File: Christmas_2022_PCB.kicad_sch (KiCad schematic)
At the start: 19 parts, among them J1 USB_A, SW1 SW_Push, SW2 SW_Push, U1 STM32F030K6Tx, U2 AMS1117-3.3

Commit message: initialised PCB
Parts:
- BT1: renamed from BT?; value Battery_Cell -> (none)
- D1, D2, D3, D4, D5: value LED -> (none)
- J1: value USB_A -> (none)
- R1, R10, R4, R5, R6, R7, R8, R9: value R -> (none)
- SW1, SW2: value SW_Push -> (none)
- U1: value STM32F030K6Tx -> (none); footprint Package_QFP:LQFP-32_7x7mm_P0.8mm -> (none)
- U2: value AMS1117-3.3 -> (none); footprint Package_TO_SOT_SMD:SOT-223-3_TabPin2 -> (none)

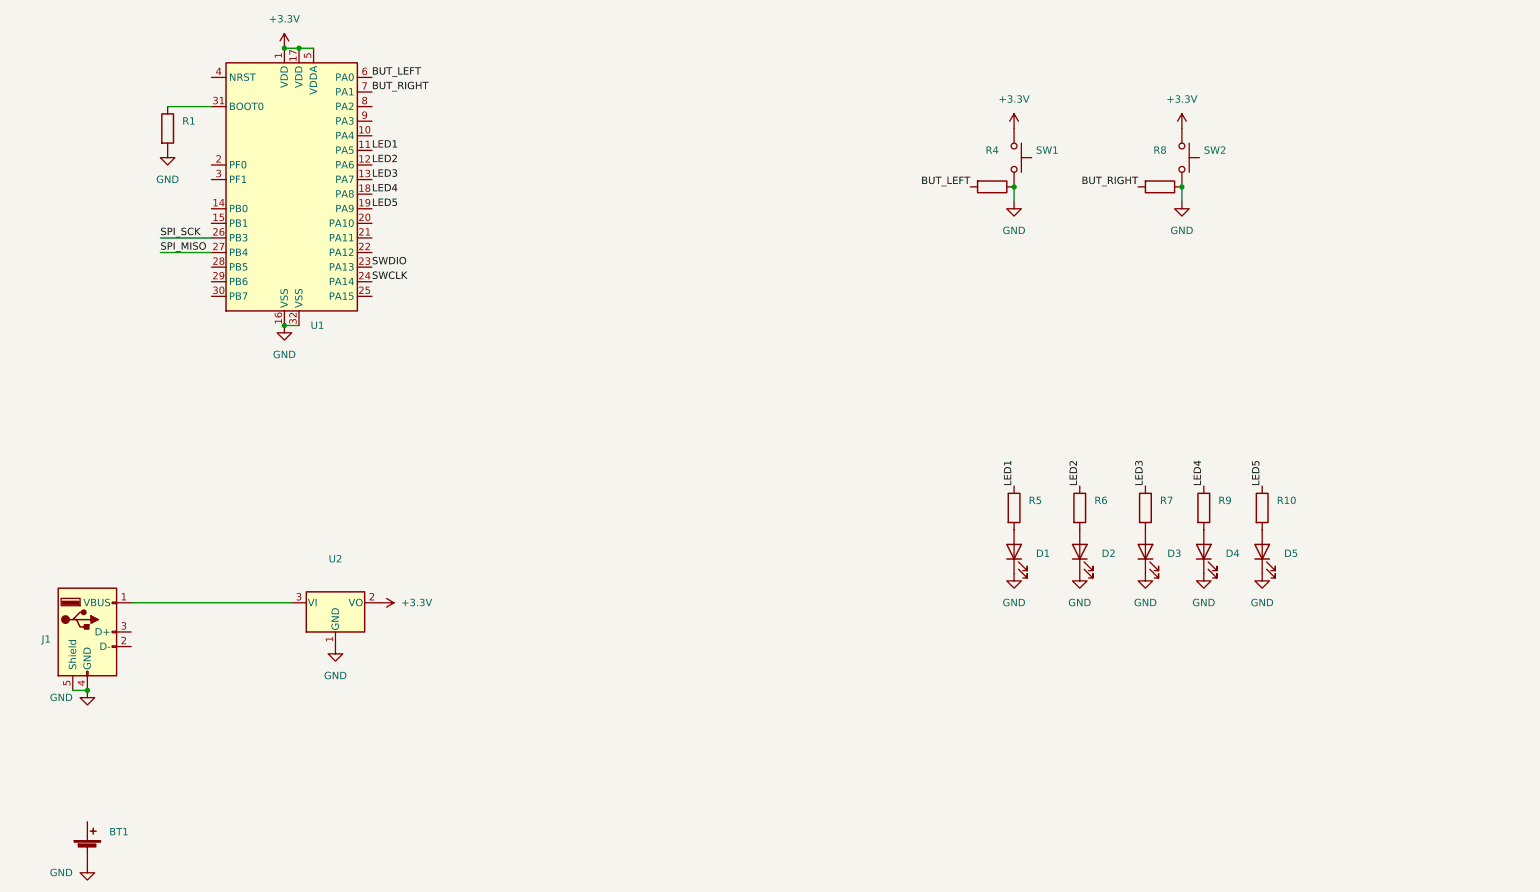
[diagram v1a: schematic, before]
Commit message: Added 3.3V slide switch
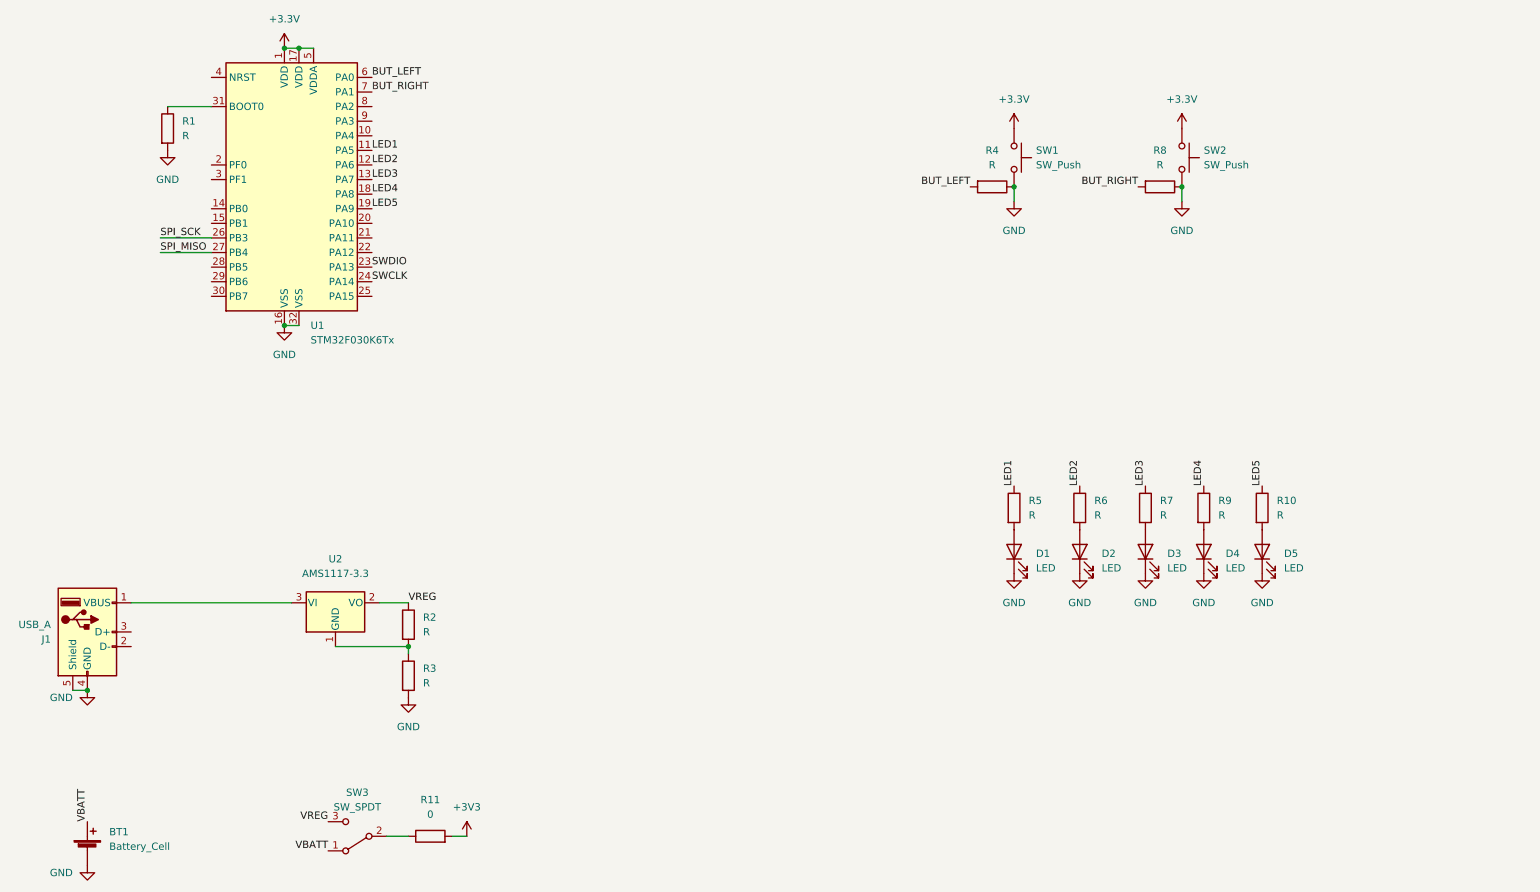
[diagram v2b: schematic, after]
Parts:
- added R11: 0, Resistor_SMD:R_0805_2012Metric_Pad1.20x1.40mm_HandSolder, symbol Device:R
- added R2, R3: R, Resistor_SMD:R_0805_2012Metric_Pad1.20x1.40mm_HandSolder, symbol Device:R
- added SW3: SW_SPDT, Button_Switch_SMD:SW_SPDT_PCM12, symbol Switch:SW_SPDT
- BT1: value (none) -> Battery_Cell; footprint (none) -> Battery:BatteryHolder_Keystone_3034_1x20mm
- D1, D2, D3, D4, D5: value (none) -> LED; footprint (none) -> LED_SMD:LED_0805_2012Metric_Pad1.15x1.40mm_HandSolder
- J1: value (none) -> USB_A; footprint (none) -> Connector_USB:USB_A_CNCTech_1001-011-01101_Horizontal
- R1, R10, R4, R5, R6, R7, R8, R9: value (none) -> R; footprint (none) -> Resistor_SMD:R_0805_2012Metric_Pad1.20x1.40mm_HandSolder
- SW1, SW2: value (none) -> SW_Push; footprint (none) -> Library:3_6_2_5mm_push_button_G_lead
- U1: value (none) -> STM32F030K6Tx; footprint (none) -> Package_QFP:LQFP-32_7x7mm_P0.8mm
- U2: value (none) -> AMS1117-3.3; footprint (none) -> Package_TO_SOT_SMD:SOT-223-3_TabPin2
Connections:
- net +3V3: now also R11.2; no longer U2.2 (VO)
- net GND: now also R3.2; no longer U2.1 (GND)
- net VBATT: now reaches BT1.1 (+)
- net VBATT: now also SW3.1 (A)
- new net: R2.2, R3.1, U2.1 (GND)
- new net: R11.1, SW3.2 (B)
- new net VREG: R2.1, SW3.3 (C), U2.2 (VO)

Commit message: completed initial layout
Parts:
- added C1, C2, C3: (no value), symbol Device:C
- added D6, D7: (no value), symbol Device:LED
- added R12, R13: (no value), symbol Device:R
- BT1: value Battery_Cell -> (none); footprint Battery:BatteryHolder_Keystone_3034_1x20mm -> (none)
- D1, D2, D3, D4, D5: value LED -> (none); footprint LED_SMD:LED_0805_2012Metric_Pad1.15x1.40mm_HandSolder -> (none)
- J1: value USB_A -> (none); footprint Connector_USB:USB_A_CNCTech_1001-011-01101_Horizontal -> (none)
- R1, R10, R2, R3, R4, R5, R6, R7, R9: value R -> (none); footprint Resistor_SMD:R_0805_2012Metric_Pad1.20x1.40mm_HandSolder -> (none)
- R11: value 0 -> (none); footprint Resistor_SMD:R_0805_2012Metric_Pad1.20x1.40mm_HandSolder -> (none)
- SW1: value SW_Push -> (none); footprint Library:3_6_2_5mm_push_button_G_lead -> (none)
- SW3: value SW_SPDT -> (none); footprint Button_Switch_SMD:SW_SPDT_PCM12 -> (none)
- U1: value STM32F030K6Tx -> (none); footprint Package_QFP:LQFP-32_7x7mm_P0.8mm -> (none)
- U2: value AMS1117-3.3 -> (none); footprint Package_TO_SOT_SMD:SOT-223-3_TabPin2 -> (none)
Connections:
- net +3V3: now also C1.1, C2.1, C3.1
- net BUT_LEFT: now also SW1.2
- net BUT_RIGHT: now also SW2.2
- net GND: now also C1.2, C2.2, C3.2, D6.1 (K), D7.1 (K); no longer SW1.2, SW2.2
- net LED6: now reaches U1.20 (PA10)
- net LED6: now also R12.1
- net LED7: now reaches U1.21 (PA11)
- net LED7: now also R13.1
- new net: D6.2 (A), R12.2
- new net: D7.2 (A), R13.2
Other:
- moved on the sheet: R4

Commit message: began routing
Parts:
- added J2, J3: SOP8_test_point, Library:sop_8_test_pad, symbol New_Library:SOP8_test_point
- R8: value R -> (none); footprint Resistor_SMD:R_0805_2012Metric_Pad1.20x1.40mm_HandSolder -> (none)
- SW2: value SW_Push -> (none); footprint Library:3_6_2_5mm_push_button_G_lead -> (none)
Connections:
- net +3V3: now also J2.1
- net GND: now also J2.2
- net SWCLK: now also J2.3
- net SWDIO: now also J2.4
- net NRST: now reaches U1.4 (NRST)
- net NRST: now also J3.2
- no-connect marks 0 -> 15
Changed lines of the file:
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@@
   (junction (at 66.04 35.56) (diameter 0) (color 0 0 0 0)
   )
+  (no_connect (at 78.74 45.72))
+  (no_connect (at 78.74 48.26))
+  (no_connect (at 78.74 50.8))
+  (no_connect (at 50.8 55.88))
+  (no_connect (at 50.8 58.42))
+  (no_connect (at 111.76 110.49))
+  (no_connect (at 111.76 115.57))
+  (no_connect (at 111.76 118.11))
+  (no_connect (at 50.8 73.66))
+  (no_connect (at 50.8 63.5))
+  (no_connect (at 50.8 66.04))
+  (no_connect (at 78.74 71.12))
+  (no_connect (at 78.74 78.74))
+  (no_connect (at 50.8 76.2))
+  (no_connect (at 50.8 78.74))
   (wire (pts (xy 29.21 147.32) (xy 26.67 147.32))
     (stroke (width 0) (type default) (color 0 0 0 0))
@@
     (stroke (width 0) (type default) (color 0 0 0 0))
   )
+  (wire (pts (xy 107.95 95.25) (xy 111.76 95.25))
+    (stroke (width 0) (type default) (color 0 0 0 0))
+  )
   (wire (pts (xy 80.01 132.08) (xy 85.09 132.08))
     (stroke (width 0) (type default) (color 0 0 0 0))
@@
     (stroke (width 0) (type default) (color 0 0 0 0))
   )
+  (wire (pts (xy 100.33 97.79) (xy 111.76 97.79))
+    (stroke (width 0) (type default) (color 0 0 0 0))
+  )
   (wire (pts (xy 92.71 172.72) (xy 95.25 172.72))
     (stroke (width 0) (type default) (color 0 0 0 0))
@@
     (stroke (width 0) (type default) (color 0 0 0 0))
   )
+  (wire (pts (xy 107.95 93.98) (xy 107.95 95.25))
+    (stroke (width 0) (type default) (color 0 0 0 0))
+  )
   (label "SPI_MISO" (at 41.91 71.12 0)
     (effects (font (size 1.27 1.27)) (justify left bottom))
@@
     (effects (font (size 1.27 1.27)) (justify left bottom))
   )
+  (label "SWCLK" (at 111.76 100.33 180)
+    (effects (font (size 1.27 1.27)) (justify right bottom))
+  )
+  (label "NRST" (at 111.76 113.03 180)
+    (effects (font (size 1.27 1.27)) (justify right bottom))
+  )
   (label "LED4" (at 223.52 111.76 90)
     (effects (font (size 1.27 1.27)) (justify left bottom))
@@
   (label "VBATT" (at 29.21 170.18 90)
     (effects (font (size 1.27 1.27)) (justify left bottom))
+  )
+  (label "NRST" (at 50.8 40.64 180)
+    (effects (font (size 1.27 1.27)) (justify right bottom))
   )
   (label "BUT_RIGHT" (at 212.09 59.69 180)
@@
     (effects (font (size 1.27 1.27)) (justify left bottom))
   )
+  (label "SWDIO" (at 111.76 102.87 180)
+    (effects (font (size 1.27 1.27)) (justify right bottom))
+  )
   (label "LED2" (at 201.93 111.76 90)
     (effects (font (size 1.27 1.27)) (justify left bottom))
@@
       (effects (font (size 1.27 1.27)) (justify right))
     )
-    (property "Value" "R" (id 1) (at 222.25 64.7699 0)
-      (effects (font (size 1.27 1.27)) (justify right))
-    )
-    (property "Footprint" "Resistor_SMD:R_0805_2012Metric_Pad1.20x1.40mm_HandSolder" (id 2) (at 221.488 63.5 90)
+    (property "Value" "" (id 1) (at 222.25 64.7699 0)
+      (effects (font (size 1.27 1.27)) (justify right))
+    )
+    (property "Footprint" "" (id 2) (at 221.488 63.5 90)
       (effects (font (size 1.27 1.27)) hide)
     )
@@
     (pin "1")
   )
+  (symbol (lib_id "New_Library:SOP8_test_point") (at 116.84 100.33 0) (unit 1)
+    (in_bom yes) (on_board yes) (fields_autoplaced)
+    (property "Reference" "J2" (id 0) (at 123.19 99.0599 0)
+      (effects (font (size 1.27 1.27)) (justify left))
+    )
+    (property "Value" "SOP8_test_point" (id 1) (at 123.19 101.5999 0)
+      (effects (font (size 1.27 1.27)) (justify left))
+    )
+    (property "Footprint" "Library:sop_8_test_pad" (id 2) (at 127 91.44 0)
+      (effects (font (size 1.27 1.27)) hide)
+    )
+    (property "Datasheet" "" (id 3) (at 116.84 100.33 0)
+      (effects (font (size 1.27 1.27)) hide)
+    )
+    (pin "2")
+    (pin "3")
+    (pin "4")
+    (pin "1")
+  )
   (symbol (lib_id "power:GND") (at 29.21 177.8 0) (unit 1)
     (in_bom yes) (on_board yes) (fields_autoplaced)
@@
     (pin "1")
   )
+  (symbol (lib_id "power:+3.3V") (at 107.95 93.98 0) (unit 1)
+    (in_bom yes) (on_board yes) (fields_autoplaced)
+    (property "Reference" "#PWR023" (id 0) (at 107.95 97.79 0)
+      (effects (font (size 1.27 1.27)) hide)
+    )
+    (property "Value" "+3.3V" (id 1) (at 107.95 88.9 0))
+    (property "Footprint" "" (id 2) (at 107.95 93.98 0)
+      (effects (font (size 1.27 1.27)) hide)
+    )
+    (property "Datasheet" "" (id 3) (at 107.95 93.98 0)
+      (effects (font (size 1.27 1.27)) hide)
+    )
+    (pin "1")
+  )
   (symbol (lib_id "Device:C") (at 115.57 50.8 0) (unit 1)
     (in_bom yes) (on_board yes) (fields_autoplaced)
@@
     )
     (property "Datasheet" "" (id 3) (at 243.84 127 0)
+      (effects (font (size 1.27 1.27)) hide)
+    )
+    (pin "1")
+  )
+  (symbol (lib_id "power:GND") (at 100.33 97.79 0) (unit 1)
+    (in_bom yes) (on_board yes) (fields_autoplaced)
+    (property "Reference" "#PWR022" (id 0) (at 100.33 104.14 0)
+      (effects (font (size 1.27 1.27)) hide)
+    )
+    (property "Value" "GND" (id 1) (at 100.33 102.87 0))
+    (property "Footprint" "" (id 2) (at 100.33 97.79 0)
+      (effects (font (size 1.27 1.27)) hide)
+    )
+    (property "Datasheet" "" (id 3) (at 100.33 97.79 0)
       (effects (font (size 1.27 1.27)) hide)
     )
@@
       (effects (font (size 1.27 1.27)) (justify left))
     )
-    (property "Value" "SW_Push" (id 1) (at 223.52 55.8799 90)
-      (effects (font (size 1.27 1.27)) (justify left))
-    )
-    (property "Footprint" "Library:3_6_2_5mm_push_button_G_lead" (id 2) (at 224.79 54.61 0)
+    (property "Value" "" (id 1) (at 223.52 55.8799 90)
+      (effects (font (size 1.27 1.27)) (justify left))
+    )
+    (property "Footprint" "" (id 2) (at 224.79 54.61 0)
       (effects (font (size 1.27 1.27)) hide)
     )
@@
     (pin "3")
   )
+  (symbol (lib_id "New_Library:SOP8_test_point") (at 116.84 115.57 0) (unit 1)
+    (in_bom yes) (on_board yes) (fields_autoplaced)
+    (property "Reference" "J3" (id 0) (at 123.19 114.2999 0)
+      (effects (font (size 1.27 1.27)) (justify left))
+    )
+    (property "Value" "SOP8_test_point" (id 1) (at 123.19 116.8399 0)
+      (effects (font (size 1.27 1.27)) (justify left))
+    )
+    (property "Footprint" "Library:sop_8_test_pad" (id 2) (at 127 106.68 0)
+      (effects (font (size 1.27 1.27)) hide)
+    )
+    (property "Datasheet" "" (id 3) (at 116.84 115.57 0)
+      (effects (font (size 1.27 1.27)) hide)
+    )
+    (pin "1")
+    (pin "2")
+    (pin "3")
+    (pin "4")
+  )
   (symbol (lib_id "Device:R") (at 254 115.57 0) (unit 1)
     (in_bom yes) (on_board yes) (fields_autoplaced)
@@
       (reference "#PWR021") (unit 1) (value "GND") (footprint "")
     )
+    (path "/7ee3bd48-2bac-409e-a3c5-a0a914fd245f"
+      (reference "#PWR022") (unit 1) (value "GND") (footprint "")
+    )
+    (path "/614fabf5-d1f0-4c94-904e-5e174f172fbe"
+      (reference "#PWR023") (unit 1) (value "+3.3V") (footprint "")
+    )
     (path "/324fdcd6-6220-42ff-aee8-8371af28628d"
       (reference "#PWR0101") (unit 1) (value "GND") (footprint "")
@@
       (reference "J1") (unit 1) (value "USB_A") (footprint "Connector_USB:USB_A_CNCTech_1001-011-01101_Horizontal")
     )
+    (path "/30a7015c-2f4f-4227-99b5-e8c70c1d0ae9"
+      (reference "J2") (unit 1) (value "SOP8_test_point") (footprint "Library:sop_8_test_pad")
+    )
+    (path "/caa89879-fd9e-498f-8e7f-e53e54aabf62"
+      (reference "J3") (unit 1) (value "SOP8_test_point") (footprint "Library:sop_8_test_pad")
+    )
     (path "/1a6796f4-a98c-4704-a590-ef7f0b3f36a9"
